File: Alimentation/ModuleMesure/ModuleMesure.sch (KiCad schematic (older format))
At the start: 65 parts, among them J1 Out Mes 1, J10 I2C 3.3V, J11 SWD, J12 ARIG Interf, J2 In Mes 1, J3 Out Mes 1, J4 In Mes 2, J5 Out Mes 1, J6 Out Mes 1, J7 In Mes 3, J8 In Mes 4, J9 I2C 5V, Q1 BSS138, Q2 BSS138, SW1 Reset, SW2 Boot0, U1 ACS711xEXLT-15AB, U2 ACS711xEXLT-15AB, U3 ACS711xEXLT-15AB, U4 ACS711xEXLT-15AB, U5 AMS1117-3.3, U6 STM32F103C8Tx, Y1 16Mhz

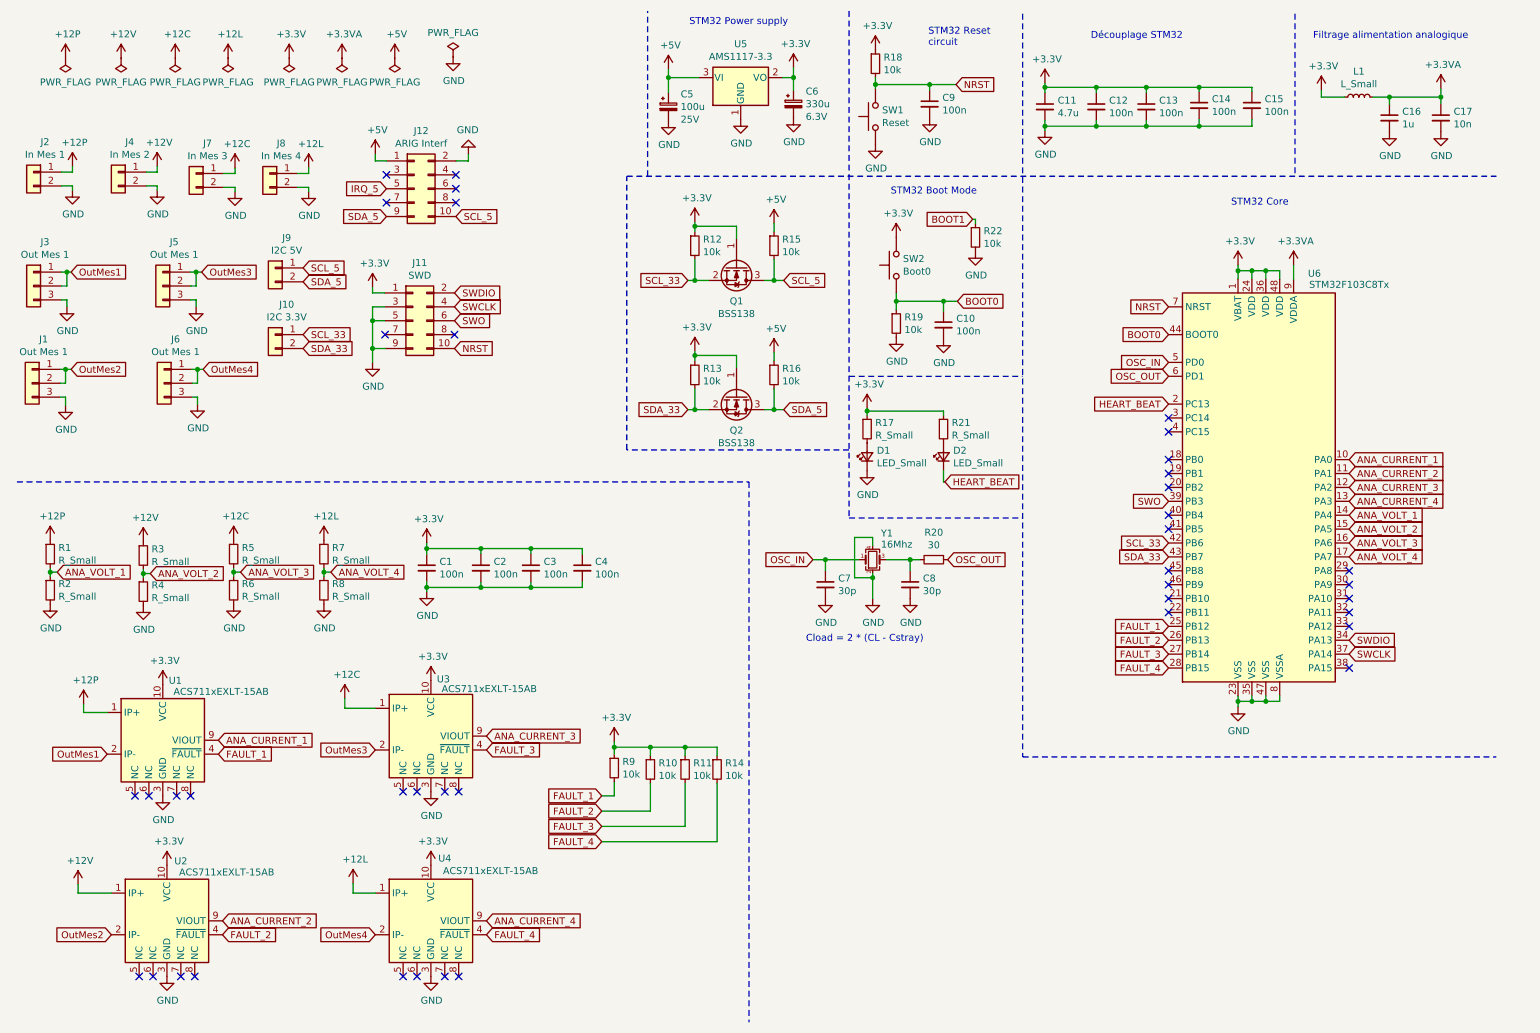
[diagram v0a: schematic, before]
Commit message: Carte de mesure de courant et de tension
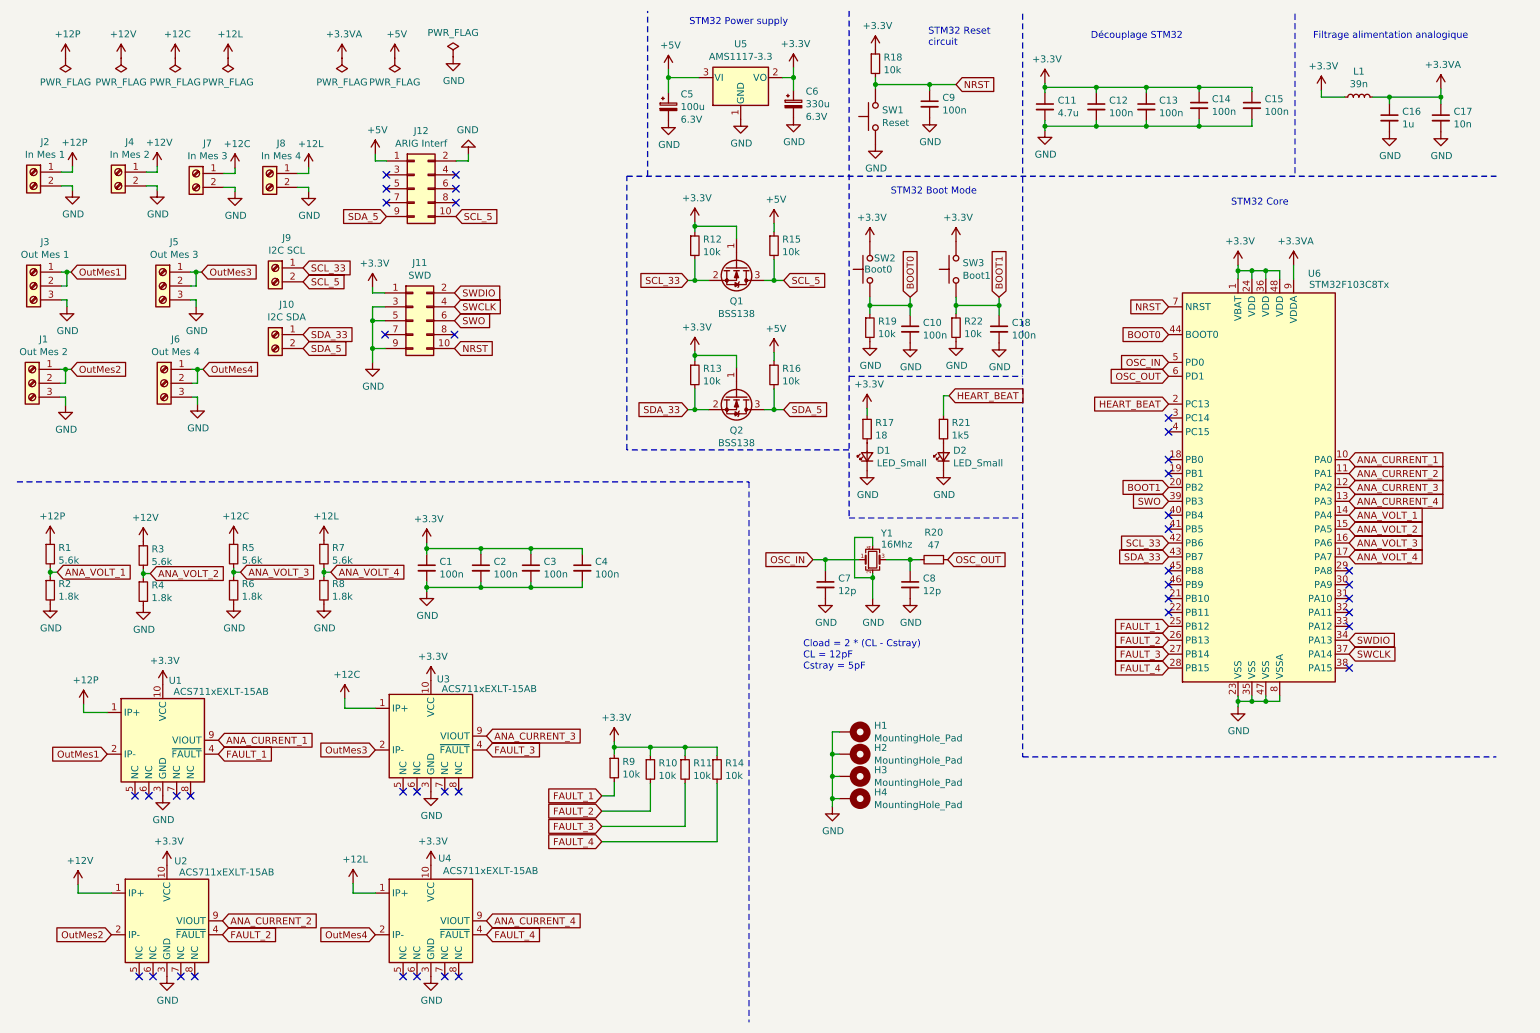
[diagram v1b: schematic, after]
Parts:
- removed J1, J3, J5, J6: Out Mes 1, symbol Connector_Generic:Conn_01x03
- removed J10: I2C 3.3V, symbol Connector_Generic:Conn_01x02
- removed J2: In Mes 1, symbol Connector_Generic:Conn_01x02
- removed J4: In Mes 2, symbol Connector_Generic:Conn_01x02
- removed J7: In Mes 3, symbol Connector_Generic:Conn_01x02
- removed J8: In Mes 4, symbol Connector_Generic:Conn_01x02
- removed J9: I2C 5V, symbol Connector_Generic:Conn_01x02
- added C18: 100n, Capacitor_SMD:C_0402_1005Metric_Pad0.74x0.62mm_HandSolder, symbol Device:C_Small
- added H1, H2, H3, H4: MountingHole_Pad, MountingHole:MountingHole_3.2mm_M3_Pad_Via, symbol Mechanical:MountingHole_Pad
- added J1: Out Mes 2, TerminalBlock_Phoenix:TerminalBlock_Phoenix_MKDS-1,5-3-5.08_1x03_P5.08mm_Horizontal, symbol Connector:Screw_Terminal_01x03
- added J10: I2C SDA, TerminalBlock_Phoenix:TerminalBlock_Phoenix_MPT-0,5-2-2.54_1x02_P2.54mm_Horizontal, symbol Connector:Screw_Terminal_01x02
- added J2: In Mes 1, TerminalBlock_Phoenix:TerminalBlock_Phoenix_MKDS-1,5-2-5.08_1x02_P5.08mm_Horizontal, symbol Connector:Screw_Terminal_01x02
- added J3: Out Mes 1, TerminalBlock_Phoenix:TerminalBlock_Phoenix_MKDS-1,5-3-5.08_1x03_P5.08mm_Horizontal, symbol Connector:Screw_Terminal_01x03
- added J4: In Mes 2, TerminalBlock_Phoenix:TerminalBlock_Phoenix_MKDS-1,5-2-5.08_1x02_P5.08mm_Horizontal, symbol Connector:Screw_Terminal_01x02
- added J5: Out Mes 3, TerminalBlock_Phoenix:TerminalBlock_Phoenix_MKDS-1,5-3-5.08_1x03_P5.08mm_Horizontal, symbol Connector:Screw_Terminal_01x03
- added J6: Out Mes 4, TerminalBlock_Phoenix:TerminalBlock_Phoenix_MKDS-1,5-3-5.08_1x03_P5.08mm_Horizontal, symbol Connector:Screw_Terminal_01x03
- added J7: In Mes 3, TerminalBlock_Phoenix:TerminalBlock_Phoenix_MKDS-1,5-2-5.08_1x02_P5.08mm_Horizontal, symbol Connector:Screw_Terminal_01x02
- added J8: In Mes 4, TerminalBlock_Phoenix:TerminalBlock_Phoenix_MKDS-1,5-2-5.08_1x02_P5.08mm_Horizontal, symbol Connector:Screw_Terminal_01x02
- added J9: I2C SCL, TerminalBlock_Phoenix:TerminalBlock_Phoenix_MPT-0,5-2-2.54_1x02_P2.54mm_Horizontal, symbol Connector:Screw_Terminal_01x02
- added SW3: Boot1, Button_Switch_SMD:SW_SPST_B3U-1000P, symbol Switch:SW_Push
- C1, C10, C12, C13, C14, C15, C2, C3, C4, C9: footprint (none) -> Capacitor_SMD:C_0402_1005Metric_Pad0.74x0.62mm_HandSolder; LCSC Part (none) -> C541405; Tension (none) -> 6.3V
- C11: footprint (none) -> Capacitor_SMD:C_0402_1005Metric_Pad0.74x0.62mm_HandSolder; LCSC Part (none) -> C87147; Tension (none) -> 6.3V
- C16: footprint (none) -> Capacitor_SMD:C_0402_1005Metric_Pad0.74x0.62mm_HandSolder; LCSC Part (none) -> C87144; Tension (none) -> 6.3V
- C17: footprint (none) -> Capacitor_SMD:C_0402_1005Metric_Pad0.74x0.62mm_HandSolder; LCSC Part (none) -> C309453; Tension (none) -> 6.3V
- C5: footprint (none) -> Capacitor_SMD:CP_Elec_5x5.4; LCSC Part (none) -> C72472; Tension 25V -> 6.3V
- C6: footprint (none) -> Capacitor_SMD:CP_Elec_6.3x7.7; LCSC Part (none) -> C58276
- C7, C8: value 30p -> 12p; footprint (none) -> Capacitor_SMD:C_0402_1005Metric_Pad0.74x0.62mm_HandSolder; Tension (none) -> 6.3V
- D1, D2: footprint (none) -> LED_SMD:LED_0805_2012Metric_Pad1.15x1.40mm_HandSolder
- J11: footprint (none) -> Connector_PinHeader_1.27mm:PinHeader_2x05_P1.27mm_Vertical_SMD
- J12: footprint (none) -> Connector_IDC:IDC-Header_2x05_P2.54mm_Vertical
- L1: value L_Small -> 39n; footprint (none) -> Inductor_SMD:L_0402_1005Metric_Pad0.77x0.64mm_HandSolder
- R1, R3, R5, R7: value R_Small -> 5.6k; footprint (none) -> Resistor_SMD:R_0805_2012Metric_Pad1.20x1.40mm_HandSolder
- R10, R11, R12, R13, R14, R15, R16, R18, R19, R22, R9: footprint (none) -> Resistor_SMD:R_0805_2012Metric_Pad1.20x1.40mm_HandSolder
- R17: value R_Small -> 18; footprint (none) -> Resistor_SMD:R_0805_2012Metric_Pad1.20x1.40mm_HandSolder
- R2, R4, R6, R8: value R_Small -> 1.8k; footprint (none) -> Resistor_SMD:R_0805_2012Metric_Pad1.20x1.40mm_HandSolder
- R20: value 30 -> 47; footprint (none) -> Resistor_SMD:R_0402_1005Metric_Pad0.72x0.64mm_HandSolder
- R21: value R_Small -> 1k5; footprint (none) -> Resistor_SMD:R_0805_2012Metric_Pad1.20x1.40mm_HandSolder
- Y1: footprint (none) -> Crystal:Crystal_SMD_3225-4Pin_3.2x2.5mm_HandSoldering; LCSC Part (none) -> C13738
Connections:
- net +12C: now also J7.1 (Pin_1)
- net +12L: now also J8.1 (Pin_1)
- net +12P: now also J2.1 (Pin_1)
- net +12V: now also J4.1 (Pin_1)
- net +3V3: now also SW3.2; no longer R21.1
- net BOOT1: now also U6.20 (PB2), C18.1, SW3.1
- net GND: now also D2.1 (K), C18.2, H1.1, H2.1, H3.1, H4.1, J1.3 (Pin_3), J2.2 (Pin_2), J3.3 (Pin_3), J4.2 (Pin_2), J5.3 (Pin_3), J6.3 (Pin_3), J7.2 (Pin_2), J8.2 (Pin_2)
- net HEART_BEAT: now also R21.1; no longer D2.1 (K)
- net OutMes1: now also J3.1 (Pin_1), J3.2 (Pin_2)
- net OutMes2: now also J1.1 (Pin_1), J1.2 (Pin_2)
- net OutMes3: now also J5.1 (Pin_1), J5.2 (Pin_2)
- net OutMes4: now also J6.1 (Pin_1), J6.2 (Pin_2)
- net SCL_33: now also J9.1 (Pin_1)
- net SCL_5: now also J9.2 (Pin_2)
- net SDA_33: now also J10.1 (Pin_1)
- net SDA_5: now also J10.2 (Pin_2)
- net IRQ_5: no longer names the net of J12.5 (Pin_5)
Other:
- note added: "Cload = 2 * (CL - Cstray)\nCL = 12pF\nCstray = 5pF"
- note removed: "Cload = 2 * (CL - Cstray)"
- moved on the sheet: C10, R19, R22, SW2
